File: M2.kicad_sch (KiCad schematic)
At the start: 0 parts

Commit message: [#82048] Add M.2 key M and key E connectors, route possible connections from the connectors
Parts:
- added A1: Mech_M2_2242_H2.5mm, antmicro-footprints:Mech_M2_2242_H2.5mm, symbol antmicroModules:Mech_M2_2242_H2.5mm
- added A2: Mech_M2_2280_H2.5mm, antmicro-footprints:Mech_M2_2280_H2.5mm, symbol antmicroModules:Mech_M2_2280_H2.5mm
- added C78, C79, C80, C81, C82, C83, C84, C85: C_220n_6V3_X7R_0402, antmicro-footprints:C_0402_1005Metric, symbol antmicroCapacitors0402:C_220n_6V3_X7R_0402
- added C86, C87, C88, C89: C_10u_0603, antmicro-footprints:C_0603_1608Metric, symbol antmicroCapacitors0603:C_10u_0603
- added C94, C95, C96, C97: C_22u_16V_0603, antmicro-footprints:C_0603_1608Metric, symbol antmicroCapacitors0603:C_22u_16V_0603
- added D15, D16 (x2): LED_G_0603_LTST-C190GKT, antmicro-footprints:LED_0603_1608Metric_G, symbol antmicroLEDIndicationDiscrete:LED_G_0603_LTST-C190GKT
- added H3, SP7: Spacer_Drill3.7mm_H2.5mm_9774025151R, antmicro-footprints:Spacer_Drill3.7mm_H2.5mm_9774025151R, symbol antmicroMechanicalParts:Spacer_Drill3.7mm_H2.5mm_9774025151R
- added J100: Bus_M.2_2199230-2, antmicro-footprints:Bus_M.2_Socket_Key_E_TE_2199230-6, symbol antmicroPciConnectors:Bus_M.2_2199230-2
- added J6: Bus_M.2_1-2199230-6, antmicro-footprints:Bus_M.2_Socket_Key_M_TE_1-2199230-6, symbol antmicroPciConnectors:Bus_M.2_1-2199230-6
- added R132, R133, R134, R137, R84, R85, R86, R96, R97: R_0R_0402, antmicro-footprints:R_0402_1005Metric, symbol antmicroResistors0402:R_0R_0402
- added R135, R136: R_10k_0402, antmicro-footprints:R_0402_1005Metric, symbol antmicroResistors0402:R_10k_0402
- added R138, R139: R_220R_0402, antmicro-footprints:R_0402_1005Metric, symbol antmicroResistors0402:R_220R_0402
- added R143: R_0R_22.4A_0603, antmicro-footprints:R_0603_1608Metric, symbol antmicroResistors0603:R_0R_22.4A_0603
- added R87, R88, R98: R_47k_0402, antmicro-footprints:R_0402_1005Metric, symbol antmicroResistors0402:R_47k_0402
- added R89: R_200R_0402, antmicro-footprints:R_0402_1005Metric, symbol antmicroResistors0402:R_200R_0402
- added R90, R99: R_4x0R_0201_array, antmicro-footprints:R_Array_4x0201_Panasonic_EXB18V, symbol antmicroResistorNetworksArrays:R_4x0R_0201_array
- added TP13, TP14, TP15, TP16, TP17, TP18, TP19: TP_0.75mm_SMD, antmicro-footprints:TP_SMD_0.75mm, symbol antmicroTestPoints:TP_0.75mm_SMD
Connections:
- new net: D16.2 (A), R138.1
- new net: J100.50 (SUSCLK), R137.1
- new net: D16.2 (A), R139.1
- new net: D15.2 (A), R89.1
- new net: D15.1 (C), J6.10 (LED)
- new net +3V3: C94.2, C95.2, C96.2, C97.2, J100.2 (3.3V), J100.4 (3.3V), J100.72 (3.3V), J100.74 (3.3V), R135.2, R136.2, R138.2, R139.2, R143.2, R87.1, R88.1, R89.2, R98.2
- new net 3V3_M2: C86.1, C87.1, C88.1, C89.1, J6.12 (3V3), J6.14 (3V3), J6.16 (3V3), J6.18 (3V3), J6.2 (3V3), J6.4 (3V3), J6.70 (3V3), J6.72 (3V3), J6.74 (3V3), R143.1
- new net C_PCIE0_TX0_N: C82.2, J6.47 (PET0_N)
- new net C_PCIE0_TX0_P: C78.2, J6.49 (PET0_P)
- new net C_PCIE0_TX1_N: C83.2, J6.35 (PET1_N)
- new net C_PCIE0_TX1_P: C79.2, J6.37 (PET1_P)
- new net C_PCIE0_TX2_N: C84.2, J6.23 (PET2_N)
- new net C_PCIE0_TX2_P: C80.2, J6.25 (PET2_P)
- new net C_PCIE0_TX3_N: C85.2, J6.11 (PET3_N)
- new net C_PCIE0_TX3_P: C81.2, J6.13 (PET3_P)
- new net GND: C86.2, C87.2, C88.2, C89.2, C94.1, C95.1, C96.1, C97.1, H3.1, J100.1 (GND), J100.18 (GND), J100.33 (GND), J100.39 (GND), J100.45 (GND), J100.51 (GND), J100.57 (GND), J100.63 (GND), J100.69 (GND), J100.7 (GND), J100.75 (GND), J100.MP, J6.1 (GND), J6.15 (GND), J6.21 (GND), J6.27 (GND), J6.3 (GND), J6.33 (GND), J6.39 (GND), J6.45 (GND), J6.51 (GND), J6.57 (GND), J6.71 (GND), J6.73 (GND), J6.75 (GND), J6.9 (GND), J6.MP1 (MP), J6.MP2 (MP), SP7.1
- new net I2S1_LRCK: R90.2 (R2.1)
- new net I2S1_SCLK: R90.1 (R1.1)
- new net I2S1_SDIN: R90.3 (R3.1)
- new net I2S1_SDOUT: R90.4 (R4.1)
- new net M2_E_I2C_CLK: R97.1
- new net M2_E_I2C_DAT: R96.1
- new net M2_E_PCM_CLK: R90.8 (R1.2)
- new net M2_E_PCM_IN: R90.6 (R3.2)
- new net M2_E_PCM_OUT: R90.5 (R4.2)
- new net M2_E_PCM_SYNC: R90.7 (R2.2)
- new net M2_E_UART_CTS: R99.7 (R2.2)
- new net M2_E_UART_RTS: R99.6 (R3.2)
- new net M2_E_UART_RX: R99.5 (R4.2)
- new net M2_E_UART_TX: R99.8 (R1.2)
- new net M2_E_W_DIS_1: TP17.1
- new net M2_E_W_DIS_2: TP18.1
- new net M2_M_SMB_CLK: J6.40 (SMB_CLK), TP15.1
- new net M2_M_SMB_DATA: J6.42 (SMB_DATA), TP14.1
- new net M2_M_SUSCLK: J6.68 (SUSCLK)
- new net PCIE_{REF}.CK+: J100.49 (REFCLK0_N)
- new net PCIE_{REF}.CK-: J100.47 (REFCLK0_P)
- new net PCIe.CLK+: J6.55 (REFCLK_P)
- new net PCIe.CLK-: J6.53 (REFCLK_N)
- new net PCIe.RX0+: J6.43 (PER0_P)
- new net PCIe.RX0-: J6.41 (PER0_N)
- new net PCIe.RX1+: J6.31 (PER1_P)
- new net PCIe.RX1-: J6.29 (PER1_N)
- new net PCIe.RX2+: J6.19 (PER2_P)
- new net PCIe.RX2-: J6.17 (PER2_N)
- new net PCIe.RX3+: J6.7 (PER3_P)
- new net PCIe.RX3-: J6.5 (PER3_N)
- new net PCIe.TX0+: C78.1
- new net PCIe.TX0-: C82.1
- new net PCIe.TX1+: C79.1
- new net PCIe.TX1-: C83.1
- new net PCIe.TX2+: C80.1
- new net PCIe.TX2-: C84.1
- new net PCIe.TX3+: C81.1
- new net PCIe.TX3-: C85.1
- new net PCIe.~{CLKREQ}: R85.1
- new net PCIe.~{RST}: R84.1
- new net PCIe_{x1}.RX0+: J100.43 (PER0_N)
- new net PCIe_{x1}.RX0-: J100.41 (PER0_P)
- new net PCIe_{x1}.TX0+: J100.37 (PET0_N)
- new net PCIe_{x1}.TX0-: J100.35 (PET0_P)
- new net SUSCLK: R137.2
- new net SYS_SCL: R97.2
- new net SYS_SDA: R96.2
- new net UART0_CTS: R99.2 (R2.1)
- new net UART0_RTS: R99.3 (R3.1)
- new net UART0_RXD: R99.4 (R4.1)
- new net UART0_TXD: R99.1 (R1.1)
- new net USB.D+: R133.1
- new net USB.D-: R134.1
- new net WIFI_BT_USB_D_N: J100.5 (USB_D_N), R134.2
- new net WIFI_BT_USB_D_P: J100.3 (USB_D_P), R133.2
- new net ~{CLKREQ}: J100.53 (~{CLKREQ0}), J6.52 (~{CLKREQ}), R136.1, R85.2, R88.2
- new net ~{LED_1}: D16.1 (C), J100.6 (~{LED_1})
- new net ~{LED_2}: D16.1 (C), J100.16 (~{LED_2})
- new net ~{M2_E_ALERT}: TP16.1
- new net ~{M2_E_UART_WAKE}: R98.1, TP19.1
- new net ~{M2_M_ALERT}: J6.44 (ALERT), TP13.1
- new net ~{PERST_D}: J100.52 (~{PERST0}), R132.2, R135.1
- new net ~{PERST}: J6.50 (~{PERST}), R132.1, R84.2, R87.2
- new net ~{PEWAKE_R}: J6.54 (~{PEWAKE}), R86.2
- new net ~{PEWAKE}: R86.1
- no-connect marks 0 -> 42
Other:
- note added: "2x PCIe x1, USB 2.0, I2C, UART and PCM"
- note added: "BT LED"
- note added: "Do we want to use 2x PCIe x1 or only one and other for eg. Oculink?"
- note added: "M.2 Gen 4 Key: M Type: Right Angle Height: 4.2mm"
- note added: "M.2 KEY E"
- note added: "M.2 KEY M"
- note added: "NOTE: Place bulk caps near to the M.2 power pads"
- note added: "PCIe x4"
- note added: "WiFi LED"

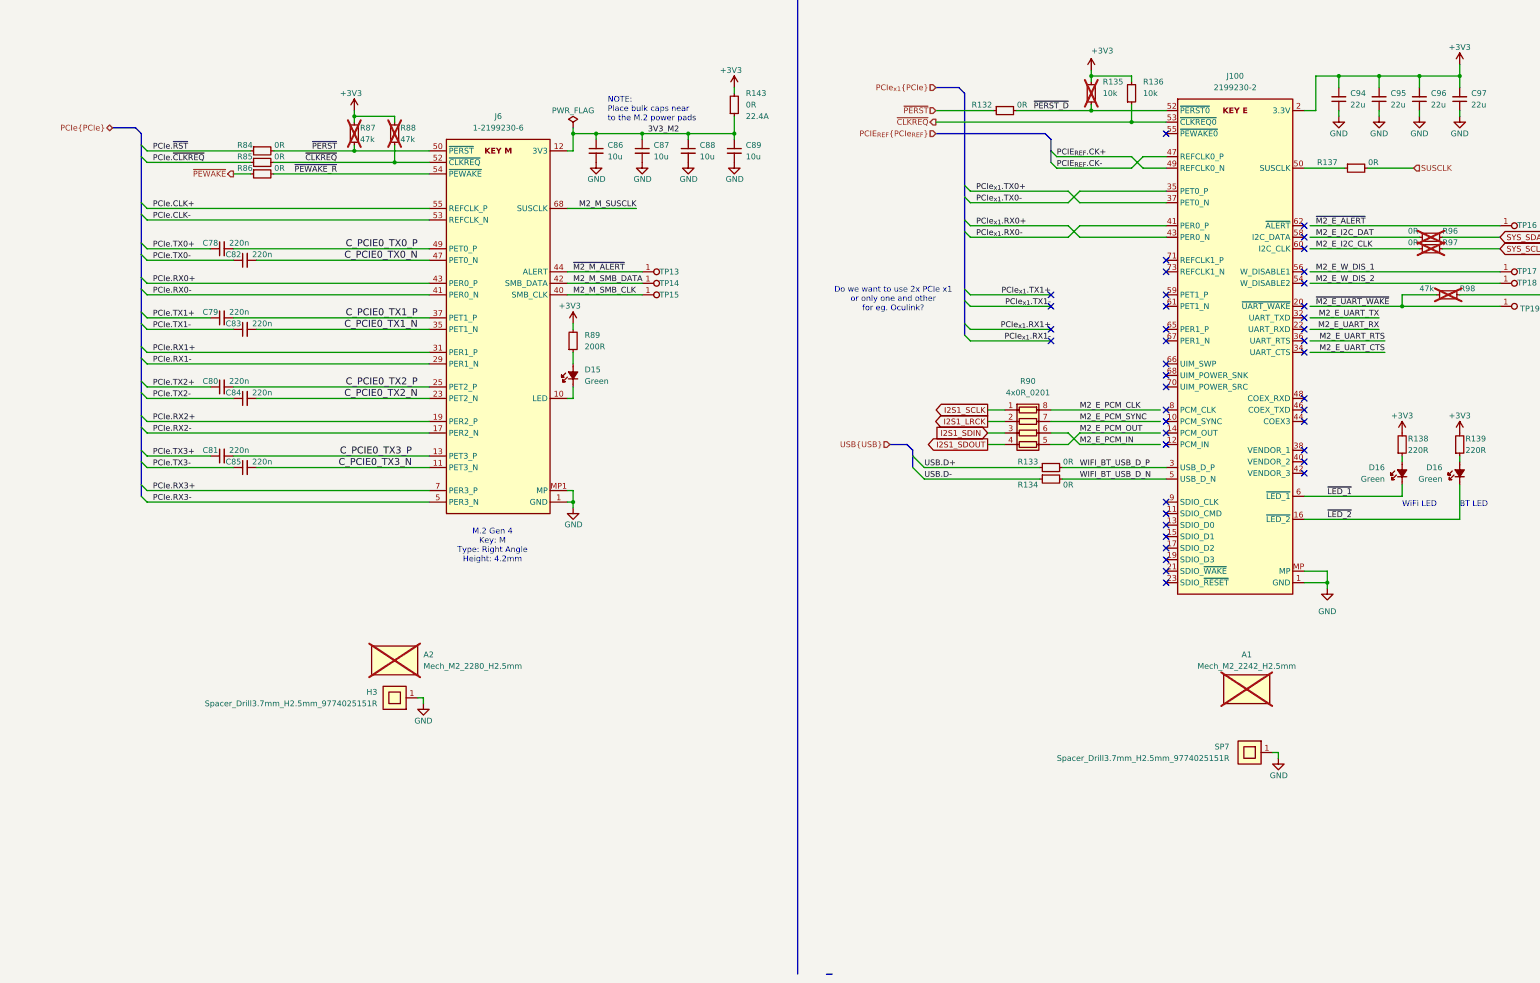
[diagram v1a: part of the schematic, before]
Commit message: [#82048] Add bus definitions and bus connections from M.2 key M to SoM
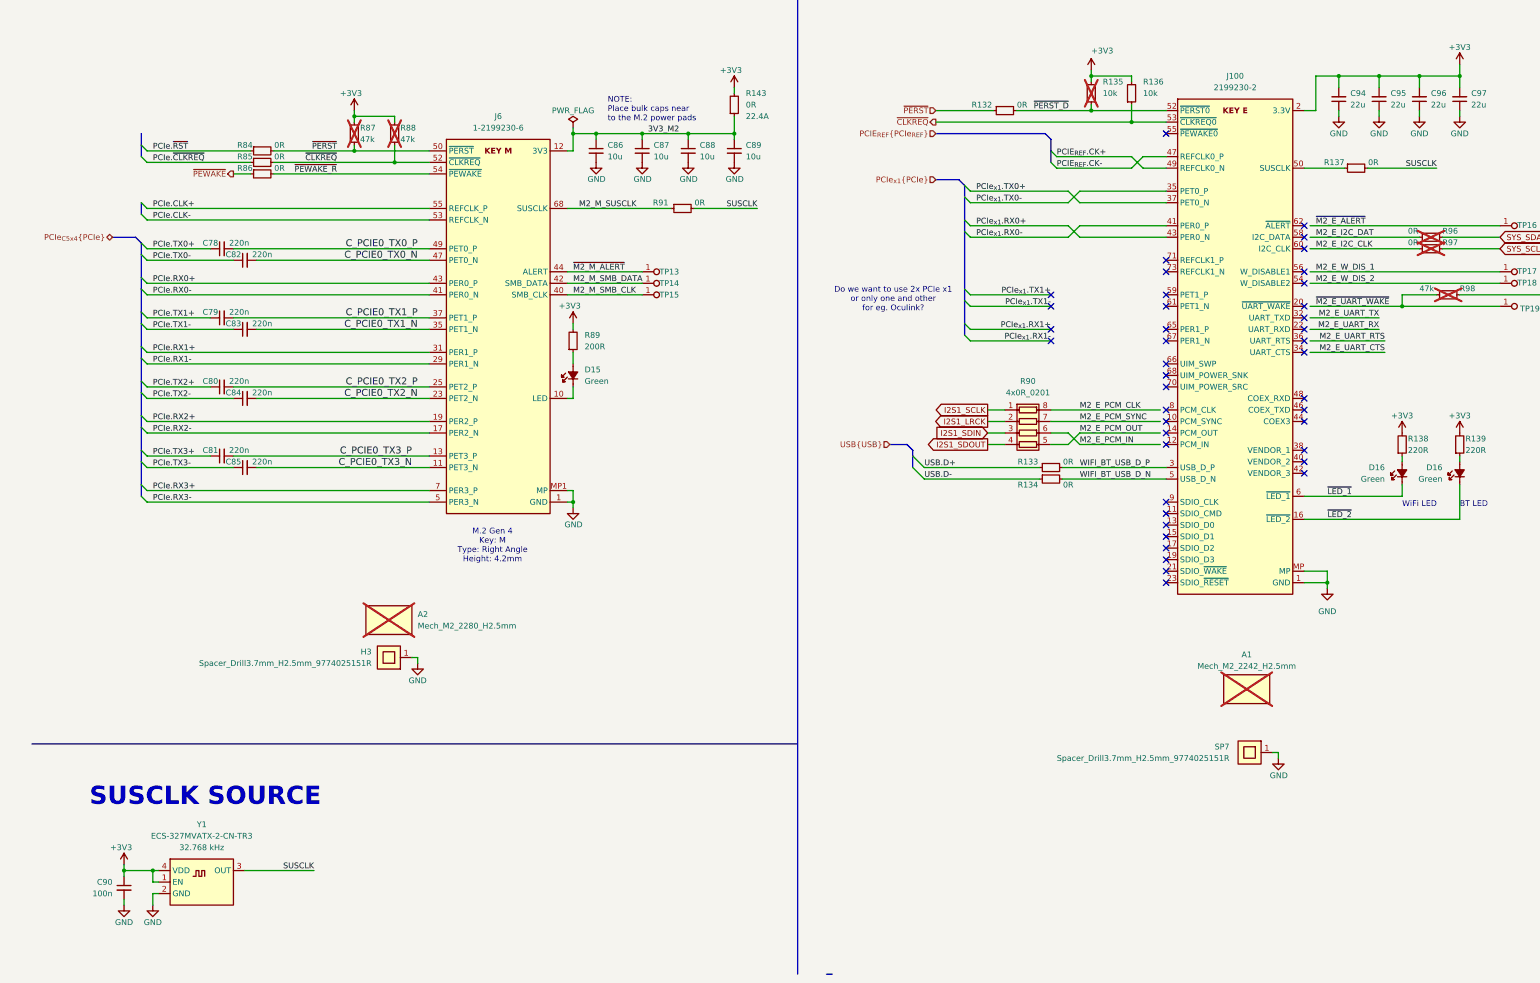
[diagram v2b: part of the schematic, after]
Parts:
- added C90: C_100n_0402, antmicro-footprints:C_0402_1005Metric, symbol antmicroCapacitors0402:C_100n_0402
- added R91: R_0R_0402, antmicro-footprints:R_0402_1005Metric, symbol antmicroResistors0402:R_0R_0402
- added Y1: Oscillator_32.768kHz_ECS_2520MV, antmicro-footprints:Oscillator_SMD_ECS_2520MV_2.5x2mm, symbol antmicroOscillators:Oscillator_32.768kHz_ECS_2520MV
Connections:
- net +3V3: now also C90.1, Y1.1 (EN), Y1.4 (VDD)
- net GND: now also C90.2, Y1.2 (GND)
- net M2_M_SUSCLK: now also R91.1
- net SUSCLK: now also R91.2, Y1.3 (OUT)
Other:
- note added: "SUSCLK SOURCE"
- moved on the sheet: A2, H3

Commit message: [#82048] Route PCIe from M.2 key E to SoM
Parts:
- removed R132: R_0R_0402, antmicro-footprints:R_0402_1005Metric, symbol antmicroResistors0402:R_0R_0402
- added R92, R93, R94: R_0R_0402, antmicro-footprints:R_0402_1005Metric, symbol antmicroResistors0402:R_0R_0402
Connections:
- net ~{PERST_D} is gone; now on net ~{PERST}: J100.52 (~{PERST0}), R135.1
- net ~{CLKREQ}: now also R93.2
- net ~{PERST}: now also R92.2
- net ~{PEWAKE_R}: now also J100.55 (~{PEWAKE0}), R94.2
- net ~{PEWAKE}: now also R94.1
- net C_PCIE0_TX0_N renamed PET0_N
- net C_PCIE0_TX0_P renamed PET0_P
- net C_PCIE0_TX1_N renamed PET1_N
- net C_PCIE0_TX1_P renamed PET1_P
- net C_PCIE0_TX2_N renamed PET2_N
- net C_PCIE0_TX2_P renamed PET2_P
- net C_PCIE0_TX3_N renamed PET3_N
- net C_PCIE0_TX3_P renamed PET3_P
- net PCIE_{REF}.CK+ renamed PCIe_{C1x1}.CK+
- net PCIE_{REF}.CK- renamed PCIe_{C1x1}.CK-
- net PCIe.CLK+ renamed PCIe_{C4x4}.CLK+
- net PCIe.CLK- renamed PCIe_{C4x4}.CLK-
- net PCIe.RX0+ renamed PCIe_{C4x4}.RX0+
- net PCIe.RX0- renamed PCIe_{C4x4}.RX0-
- net PCIe.RX1+ renamed PCIe_{C4x4}.RX1+
- net PCIe.RX1- renamed PCIe_{C4x4}.RX1-
- net PCIe.RX2+ renamed PCIe_{C4x4}.RX2+
- net PCIe.RX2- renamed PCIe_{C4x4}.RX2-
- net PCIe.RX3+ renamed PCIe_{C4x4}.RX3+
- net PCIe.RX3- renamed PCIe_{C4x4}.RX3-
- net PCIe.TX0+ renamed PCIe_{C4x4}.TX0+
- net PCIe.TX0- renamed PCIe_{C4x4}.TX0-
- net PCIe.TX1+ renamed PCIe_{C4x4}.TX1+
- net PCIe.TX1- renamed PCIe_{C4x4}.TX1-
- net PCIe.TX2+ renamed PCIe_{C4x4}.TX2+
- net PCIe.TX2- renamed PCIe_{C4x4}.TX2-
- net PCIe.TX3+ renamed PCIe_{C4x4}.TX3+
- net PCIe.TX3- renamed PCIe_{C4x4}.TX3-
- net PCIe.~{CLKREQ} renamed PCIe_{C4x4}.~{CLKREQ}
- net PCIe.~{RST} renamed PCIe_{C4x4}.~{RST}
- net PCIe_{x1}.RX0+ renamed PCIe_{C1x1}.RX0+
- net PCIe_{x1}.RX0- renamed PCIe_{C1x1}.RX0-
- net PCIe_{x1}.TX0+ renamed PCIe_{C1x1}.TX0+
- net PCIe_{x1}.TX0- renamed PCIe_{C1x1}.TX0-
- new net PCIe_{C1x1}.~{CLKREQ}: R93.1
- new net PCIe_{C1x1}.~{RST}: R92.1
- no-connect marks 42 -> 43
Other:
- moved on the sheet: C78, C79, C80, C81, C82, C83, C84, C85, R99

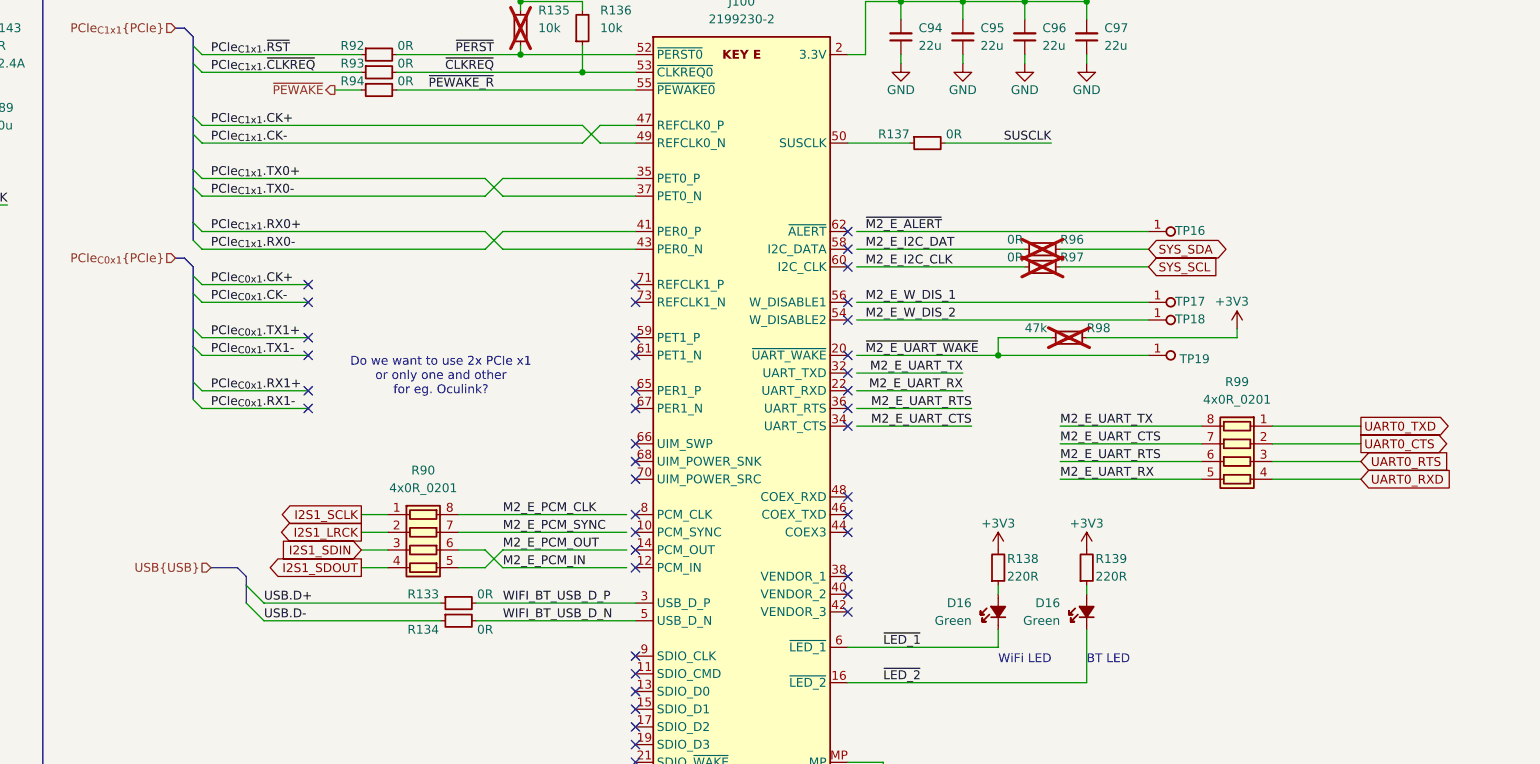
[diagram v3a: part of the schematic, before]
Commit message: [#82048] Route UART, I2S and I2C from M.2 key E to SoM
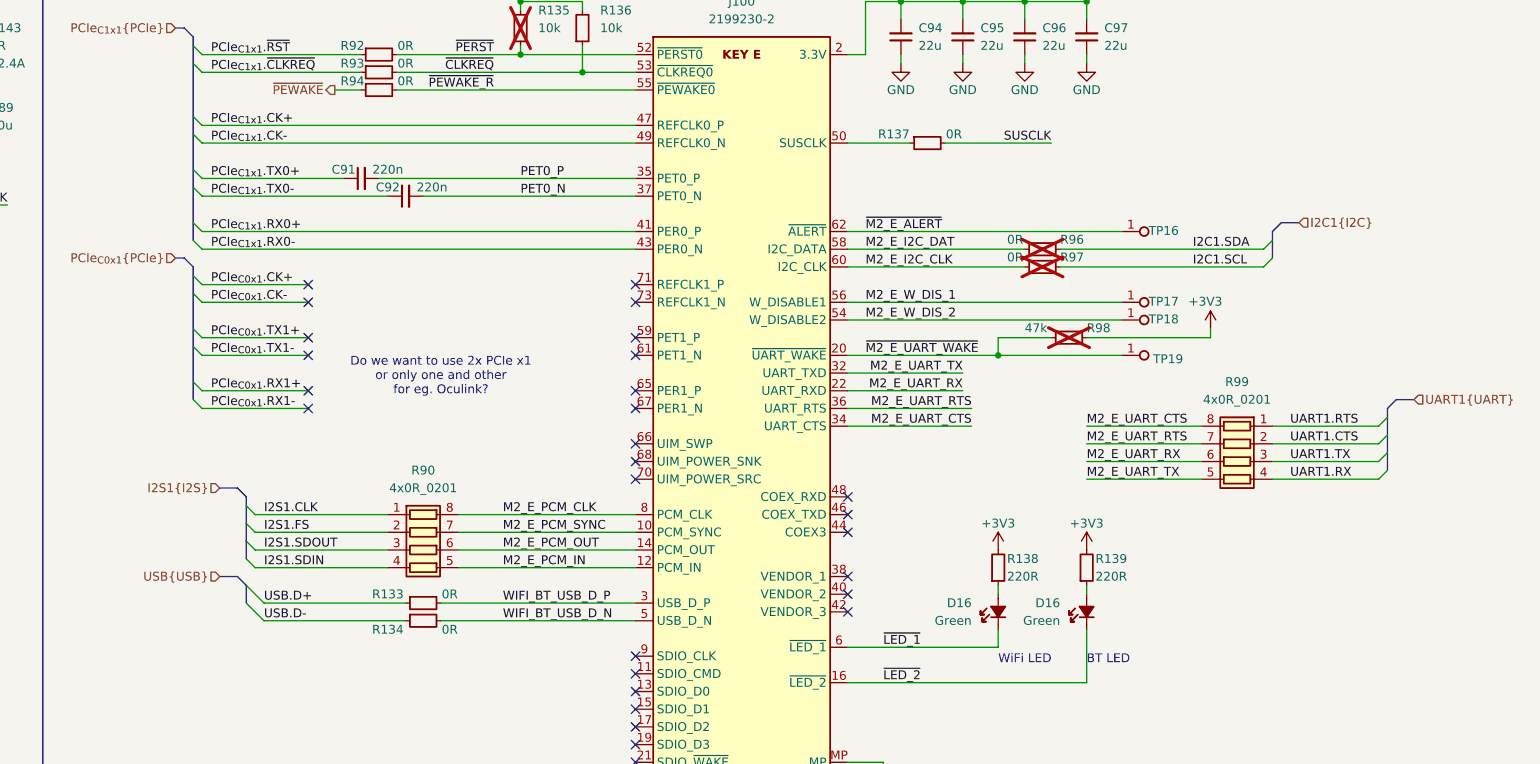
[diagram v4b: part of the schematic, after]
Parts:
- added C91, C92: C_220n_6V3_X7R_0402, antmicro-footprints:C_0402_1005Metric, symbol antmicroCapacitors0402:C_220n_6V3_X7R_0402
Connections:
- net M2_E_I2C_CLK: now also J100.60 (I2C_CLK)
- net M2_E_I2C_DAT: now also J100.58 (I2C_DATA)
- net M2_E_PCM_CLK: now also J100.8 (PCM_CLK)
- net M2_E_PCM_IN: now also J100.12 (PCM_IN), R90.5 (R4.2); no longer R90.6 (R3.2)
- net M2_E_PCM_OUT: now also J100.14 (PCM_OUT), R90.6 (R3.2); no longer R90.5 (R4.2)
- net M2_E_PCM_SYNC: now also J100.10 (PCM_SYNC)
- net M2_E_UART_CTS: now also J100.34 (UART_CTS), R99.8 (R1.2); no longer R99.7 (R2.2)
- net M2_E_UART_RTS: now also J100.36 (UART_RTS), R99.7 (R2.2); no longer R99.6 (R3.2)
- net M2_E_UART_RX: now also J100.22 (UART_RXD), R99.6 (R3.2); no longer R99.5 (R4.2)
- net M2_E_UART_TX: now also J100.32 (UART_TXD), R99.5 (R4.2); no longer R99.8 (R1.2)
- net M2_E_W_DIS_1: now also J100.56 (W_DISABLE1)
- net M2_E_W_DIS_2: now also J100.54 (W_DISABLE2)
- net PCIe_{C1x1}.CK+: now also J100.47 (REFCLK0_P); no longer J100.49 (REFCLK0_N)
- net PCIe_{C1x1}.CK-: now also J100.49 (REFCLK0_N); no longer J100.47 (REFCLK0_P)
- net PCIe_{C1x1}.RX0+: now also J100.41 (PER0_P); no longer J100.43 (PER0_N)
- net PCIe_{C1x1}.RX0-: now also J100.43 (PER0_N); no longer J100.41 (PER0_P)
- net PCIe_{C1x1}.TX0+: now also C91.1; no longer J100.37 (PET0_N)
- net PCIe_{C1x1}.TX0-: now also C92.1; no longer J100.35 (PET0_P)
- net PET0_N: now also J100.37 (PET0_N), C92.2
- net PET0_P: now also J100.35 (PET0_P), C91.2
- net ~{M2_E_ALERT}: now also J100.62 (~{ALERT})
- net ~{M2_E_UART_WAKE}: now also J100.20 (~{UART_WAKE})
- net I2S1_LRCK renamed I2S1.FS
- net I2S1_SCLK renamed I2S1.CLK
- net I2S1_SDIN renamed I2S1.SDOUT
- net I2S1_SDOUT renamed I2S1.SDIN
- net SYS_SCL renamed I2C1.SCL
- net SYS_SDA renamed I2C1.SDA
- net UART0_CTS renamed UART1.CTS
- net UART0_RTS renamed UART1.TX
- net UART0_RXD renamed UART1.RX
- net UART0_TXD renamed UART1.RTS
- no-connect marks 43 -> 29
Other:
- moved on the sheet: R133, R134, TP16, TP17, TP18, TP19
